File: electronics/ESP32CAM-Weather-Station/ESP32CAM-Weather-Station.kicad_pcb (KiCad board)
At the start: 4 copper layers, 100 x 100 mm, 94 parts, among them IC1 BME688, IC2 SGP41-D-R4, IC3 VEML7700-TT, IC4 BQ24093DGQR, IC5 BQ29707DSET, IC6 MCP3426A0T-E_SN, IC7 TPS63070RNMR, J1 B4B-PH-SM4-TB_LF__SN_, J10 Conn_01x02_Pin, J2 B4B-PH-SM4-TB_LF__SN_, J3 B4B-PH-SM4-TB_LF__SN_, J4 B4B-PH-SM4-TB_LF__SN_, J5 Conn_01x04_Socket, J6 XT30UPB-M, J7 Conn_01x02_Pin, J8 Conn_01x02_Pin, J9 Conn_01x02_Pin, Q2 CSD16406Q3, Q3 CSD16406Q3, U1 ESP32-CAM, U2 TPS631000DRLR, U3 GDT25-07-S1-RP

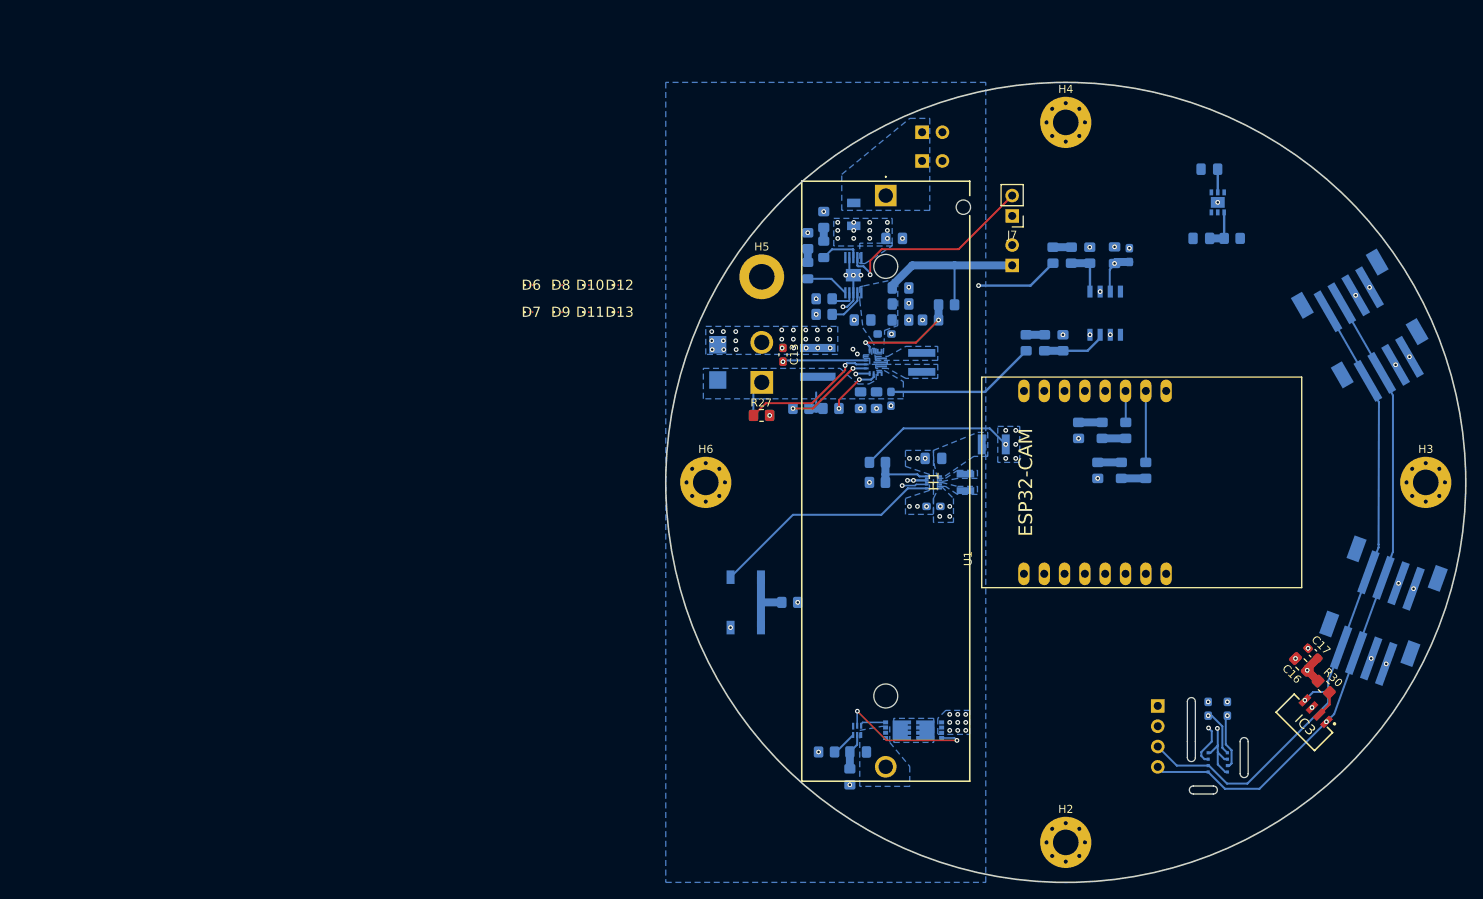
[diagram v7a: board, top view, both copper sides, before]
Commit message: [Ready for review, Passes DRC] Routing completed.
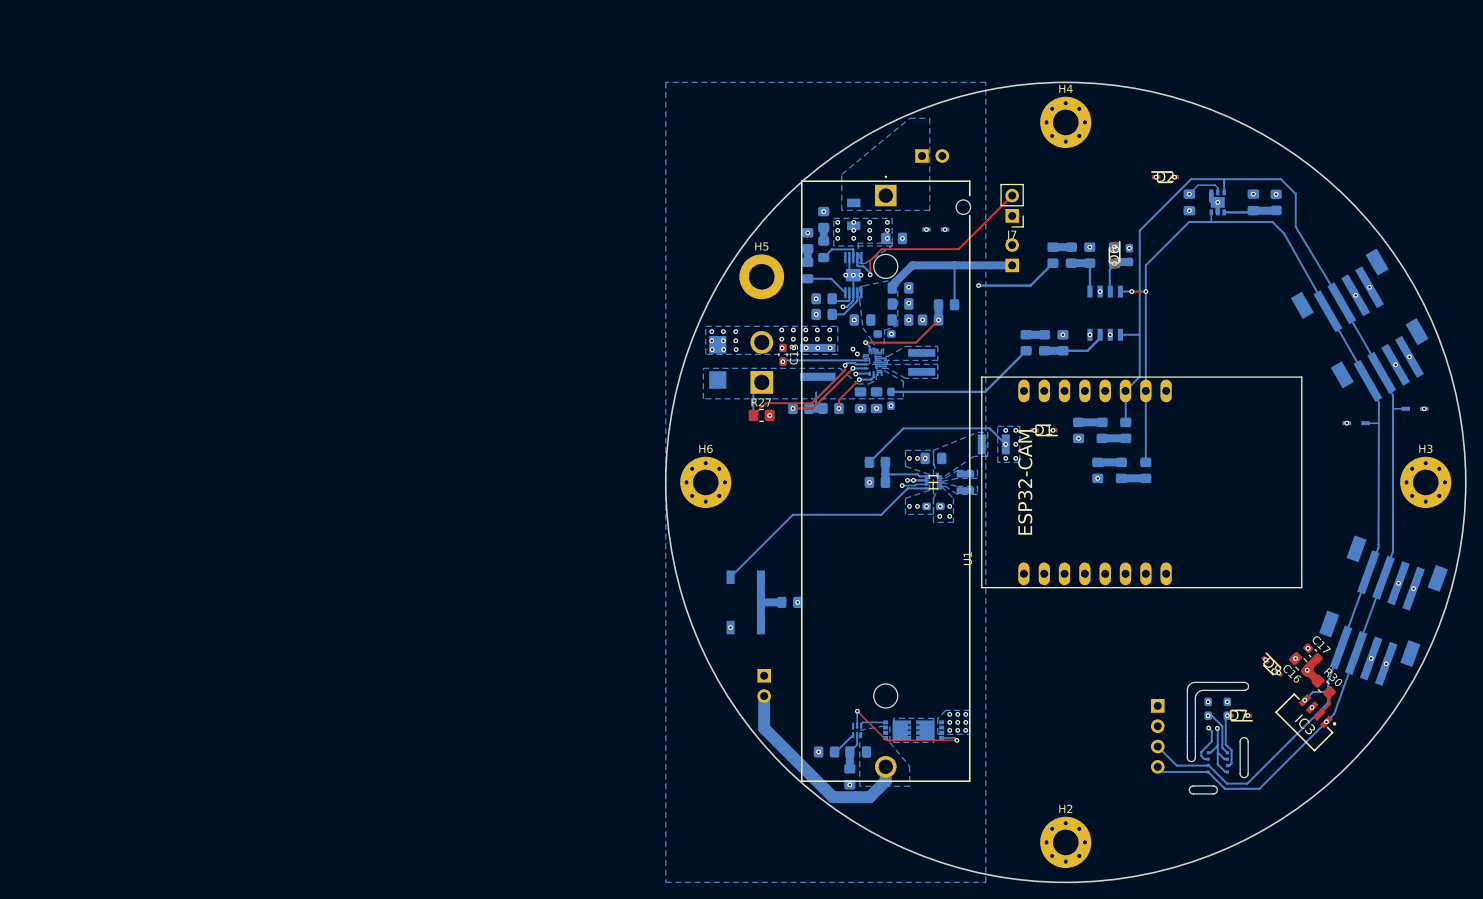
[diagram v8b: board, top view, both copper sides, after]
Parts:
- removed D12, D13: ESDZV5H-1BU2, ESDZV5H-1BU2:ESDZV5H1BU2
- added D1: SD05C-7, SD05C-7:SOD2513X120N, F.Cu at (147.2, 93.5)
- added D2: SD05C-7, SD05C-7:SOD2513X120N, F.Cu at (162.4, 61.9)
- D10, D11, D9: value ESDZV5H-1BU2 -> SD05C-7; footprint ESDZV5H-1BU2:ESDZV5H1BU2 -> SD05C-7:SOD2513X120N; moved to B.Cu
- D6, D7, D8: value ESDZV5H-1BU2 -> SD05C-7; footprint ESDZV5H-1BU2:ESDZV5H1BU2 -> SD05C-7:SOD2513X120N
- moved D10 104.3 mm to (193.7, 90.8), turned to 180 degrees
- moved D7 101.8 mm to (171.6, 129.2), turned to 180 degrees
- moved D8 100.9 mm to (175.8, 123.0), turned to -45 degrees
- moved D9 100.4 mm to (186.3, 92.6)
- moved D6 73.0 mm to (156.1, 71.6), turned to -90 degrees
- moved J9 67.3 mm to (112.3, 124.2), turned to 180 degrees
- moved D11 44.4 mm to (133.8, 68.4), turned to 180 degrees
- moved C18 7.91 mm to (173.4, 65.0), turned to 90 degrees
- moved R31 7.11 mm to (176.3, 65.0), turned to -90 degrees
- moved C19 4.84 mm to (165.4, 65.0), turned to -90 degrees
- moved J8 2.97 mm to (132.0, 59.2)
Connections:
- D10 pad 2: +3.3V -> /I2C_SCL
- D11 pad 2: /I2C_SDA -> +VBAT
- D9 pad 1: +3.3V -> GND
- D9 pad 2: GND -> /I2C_SDA
- IC2 pad 3: unconnected-(IC2-SDA-Pad3) -> /I2C_SDA
- J9 pad 1: +VBAT_UNFUSED -> +VBAT
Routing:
- net /I2C_SCL: track 85.3 -> 149.9 mm
- net /I2C_SDA: track 91.4 -> 144.6 mm, vias 1 -> 3
- net -VBAT: track 0.00 -> 25.4 mm
- net GND: track 20.7 -> 23.8 mm, vias 81 -> 90
- net +3.3V: track 50.4 -> 52.3 mm, vias 17 -> 22
- net /SGP41_VDD_TAP: track 5.06 -> 6.60 mm
- net +VBAT: vias 22 -> 23
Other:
- outline, holes or cut-outs redrawn
